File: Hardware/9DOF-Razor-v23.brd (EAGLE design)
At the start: 40.6 x 27.9 mm, 41 parts, among them J1 AVR_SPI_PRG_6PTH, Q1 8MHz, U1 ITG-32001:1, U2 ADXL3451:1, U5 3.3V, U6 ATMEGA328

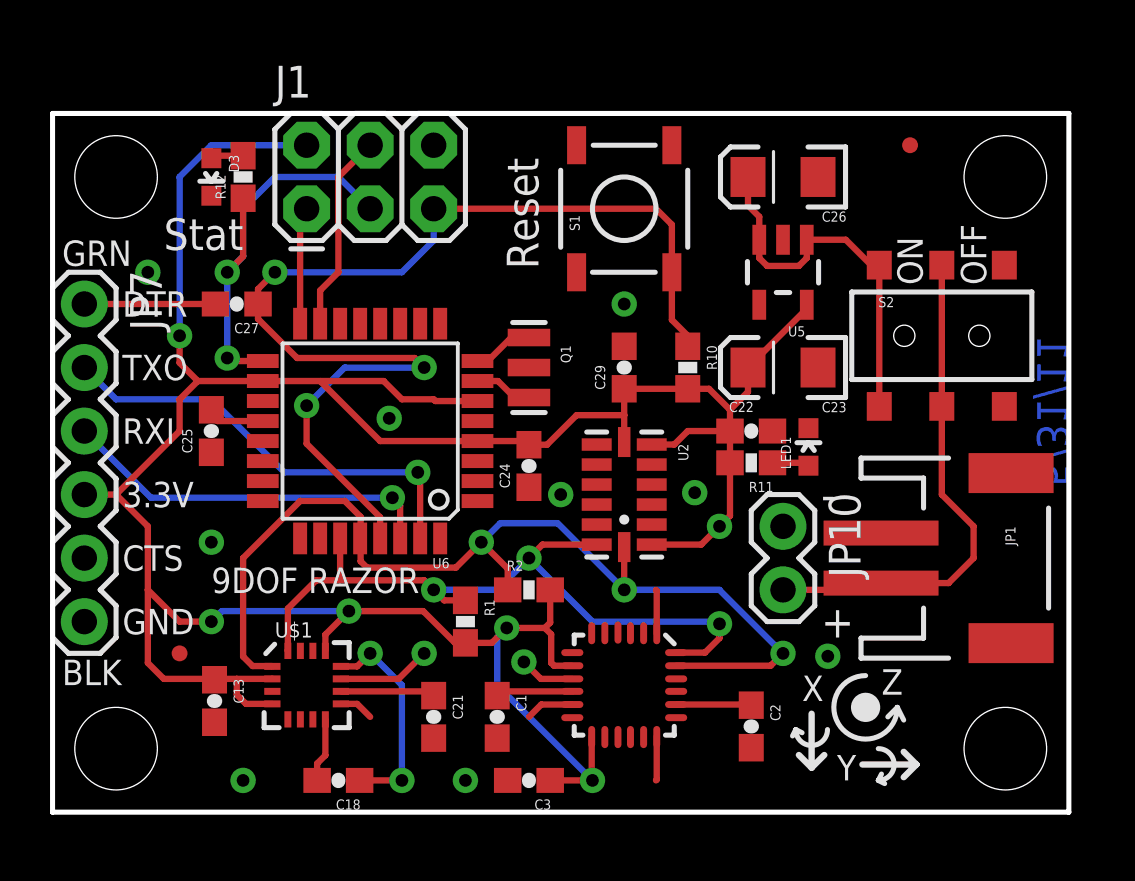
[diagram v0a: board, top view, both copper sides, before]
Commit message: General cleanup in schematic
Added:
- Rev code on PCB
- Minor trace cleanup on mag IC
Replaced:
- Net labels with flag style markers
- Old Frame design with new Frame design that includes CC3.0 and OSHW
stuff
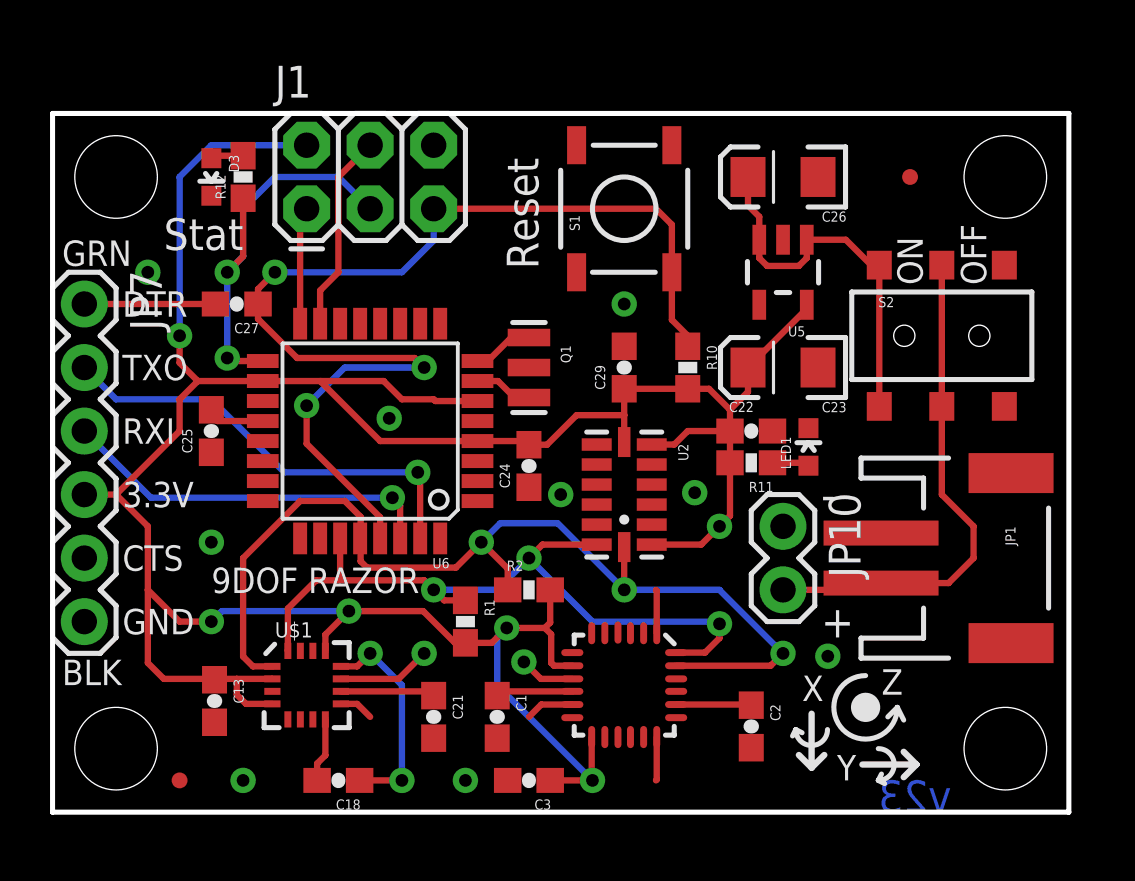
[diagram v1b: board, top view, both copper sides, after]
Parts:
- removed U$3: CREATIVE_COMMONS, SparkFun:CREATIVE_COMMONS
- moved JP12 5.08 mm to (5.08, 1.27)
- moved JP11 1.27 mm to (34.3, 25.4)
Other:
- board text added: "v23"
- board text removed: "5/31/11"
- board text removed: "Kade Jensen"
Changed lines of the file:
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@@
 <text x="5.842" y="12.192" size="1.016" layer="22" font="vector" ratio="15" rot="MR0">3.3V</text>
 <text x="5.334" y="9.652" size="1.016" layer="22" font="vector" ratio="15" rot="MR0">CTS</text>
-<text x="40.64" y="19.05" size="1.27" layer="16" font="vector" ratio="19" rot="MR270">5/31/11</text>
+<text x="33.02" y="1.27" size="1.27" layer="16" font="vector" ratio="19" rot="MR180">v23</text>
 <wire x1="33.02" y1="2.54" x2="33.02" y2="1.27" width="0.2032" layer="21" curve="-180"/>
 <wire x1="33.02" y1="1.27" x2="33.274" y2="1.143" width="0.2032" layer="21"/>
@@
 <rectangle x1="24.384" y1="6.985" x2="24.638" y2="7.239" layer="41"/>
 <rectangle x1="24.384" y1="2.921" x2="24.638" y2="3.175" layer="41"/>
-<text x="21.59" y="-11.43" size="1.778" layer="27" font="fixed" ratio="10">Kade Jensen</text>
 </plain>
 <attributes>
@@
 <element name="U2" library="Testing" package="LGA14" value="ADXL3451:1" x="22.86" y="12.7" rot="R270"/>
 <element name="U$1" library="SparkFun" package="16LPCC" value="HMC5883LSMD" x="10.16" y="5.08"/>
-<element name="U$3" library="SparkFun" package="CREATIVE_COMMONS" value="CREATIVE_COMMONS" x="-8.89" y="-11.43"/>
 <element name="U$4" library="SparkFun" package="OSHW-LOGO-L" value="OSHW-LOGOL" x="20.32" y="4.445" rot="MR0"/>
-<element name="JP11" library="abes" package="FIDUCIAL-1X2.5" value="FIDUCIAL1X2.5" x="34.29" y="26.67"/>
-<element name="JP12" library="abes" package="FIDUCIAL-1X2.5" value="FIDUCIAL1X2.5" x="5.08" y="6.35"/>
+<element name="JP11" library="abes" package="FIDUCIAL-1X2.5" value="FIDUCIAL1X2.5" x="34.29" y="25.4"/>
+<element name="JP12" library="abes" package="FIDUCIAL-1X2.5" value="FIDUCIAL1X2.5" x="5.08" y="1.27"/>
 </elements>
 <signals>
@@
 <wire x1="12.319" y1="10.033" x2="12.573" y2="9.779" width="0.254" layer="1"/>
 <wire x1="12.573" y1="9.779" x2="16.129" y2="9.779" width="0.254" layer="1"/>
-<wire x1="8.001" y1="5.842" x2="7.62" y2="6.223" width="0.254" layer="1"/>
-<wire x1="8.778" y1="5.842" x2="8.001" y2="5.842" width="0.254" layer="1"/>
-<wire x1="8.79" y1="5.83" x2="8.778" y2="5.842" width="0.254" layer="1"/>
 <wire x1="9.906" y1="12.446" x2="7.62" y2="10.16" width="0.254" layer="1"/>
 <wire x1="7.62" y1="10.16" x2="7.62" y2="6.223" width="0.254" layer="1"/>
@@
 <wire x1="17.145" y1="10.795" x2="18.2" y2="9.74" width="0.254" layer="1"/>
 <wire x1="18.2" y1="9.74" x2="18.2" y2="8.89" width="0.254" layer="1"/>
+<wire x1="8.79" y1="5.83" x2="8.013" y2="5.83" width="0.254" layer="1"/>
+<wire x1="8.013" y1="5.83" x2="7.62" y2="6.223" width="0.254" layer="1"/>
 </signal>
 <signal name="SDA">
